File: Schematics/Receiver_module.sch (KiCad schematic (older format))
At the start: 17 parts, among them J1 I2C_ToTagger, T1 BC237, T2 BC237, T3 BC237

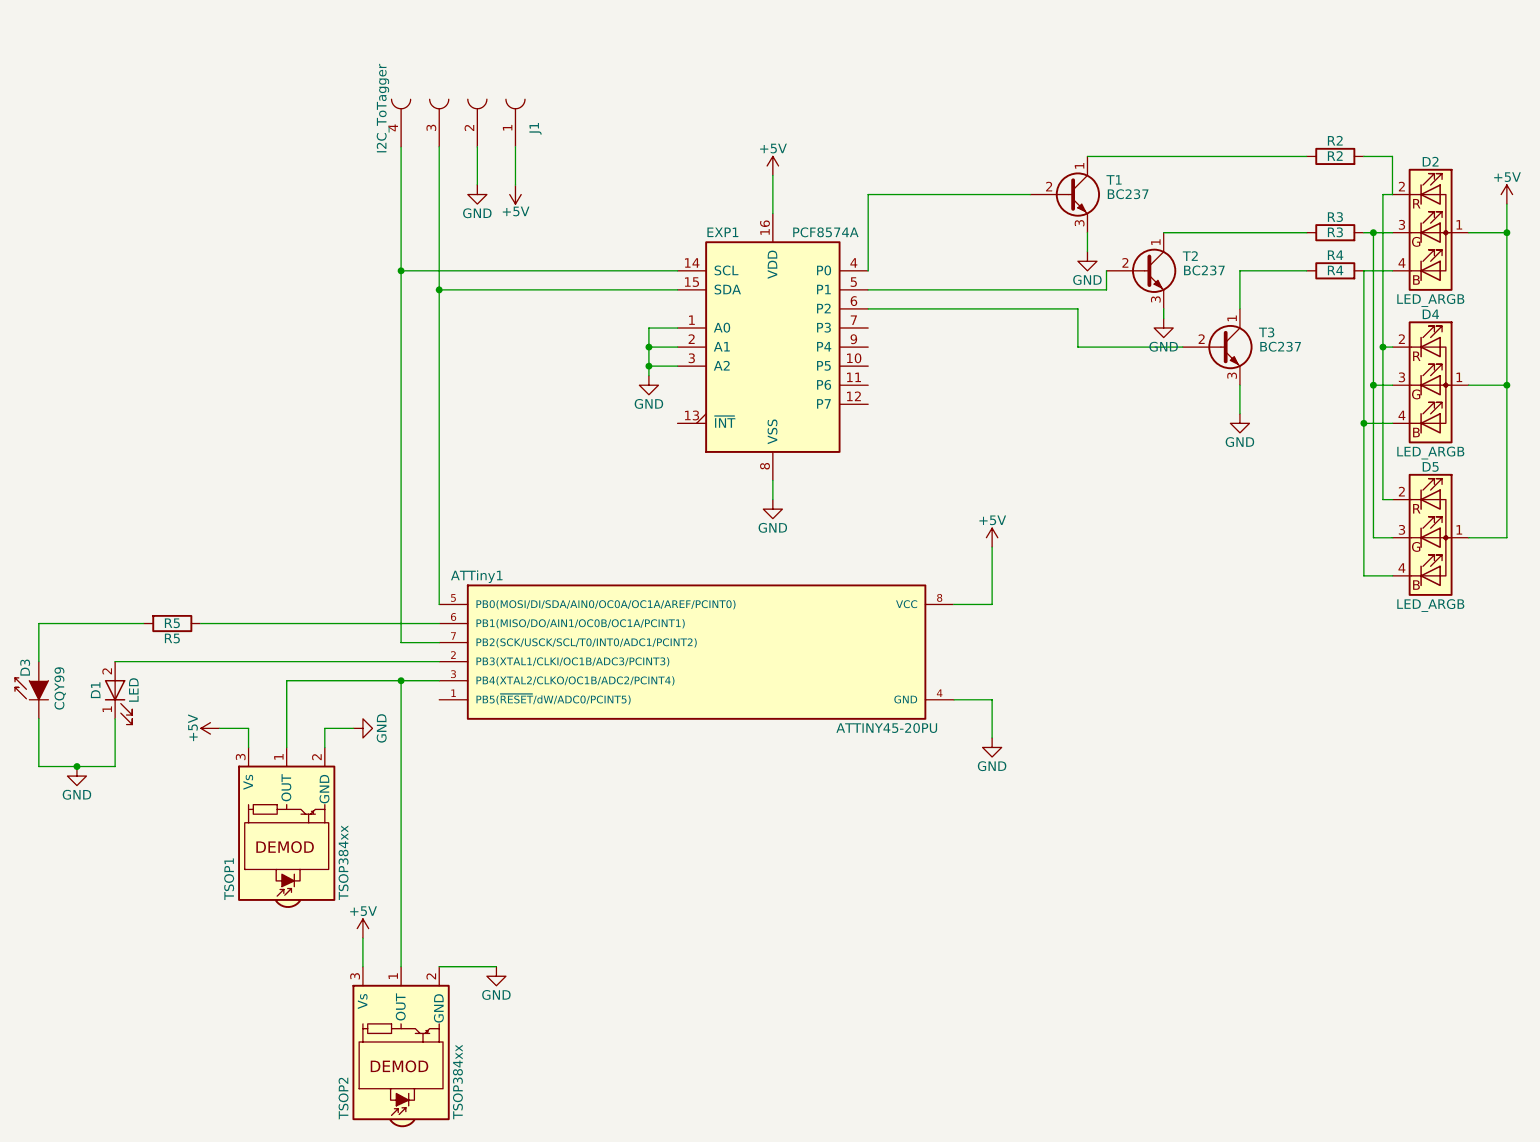
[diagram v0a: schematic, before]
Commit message: New Version of Tagger/Receiver Schematics and PCBs
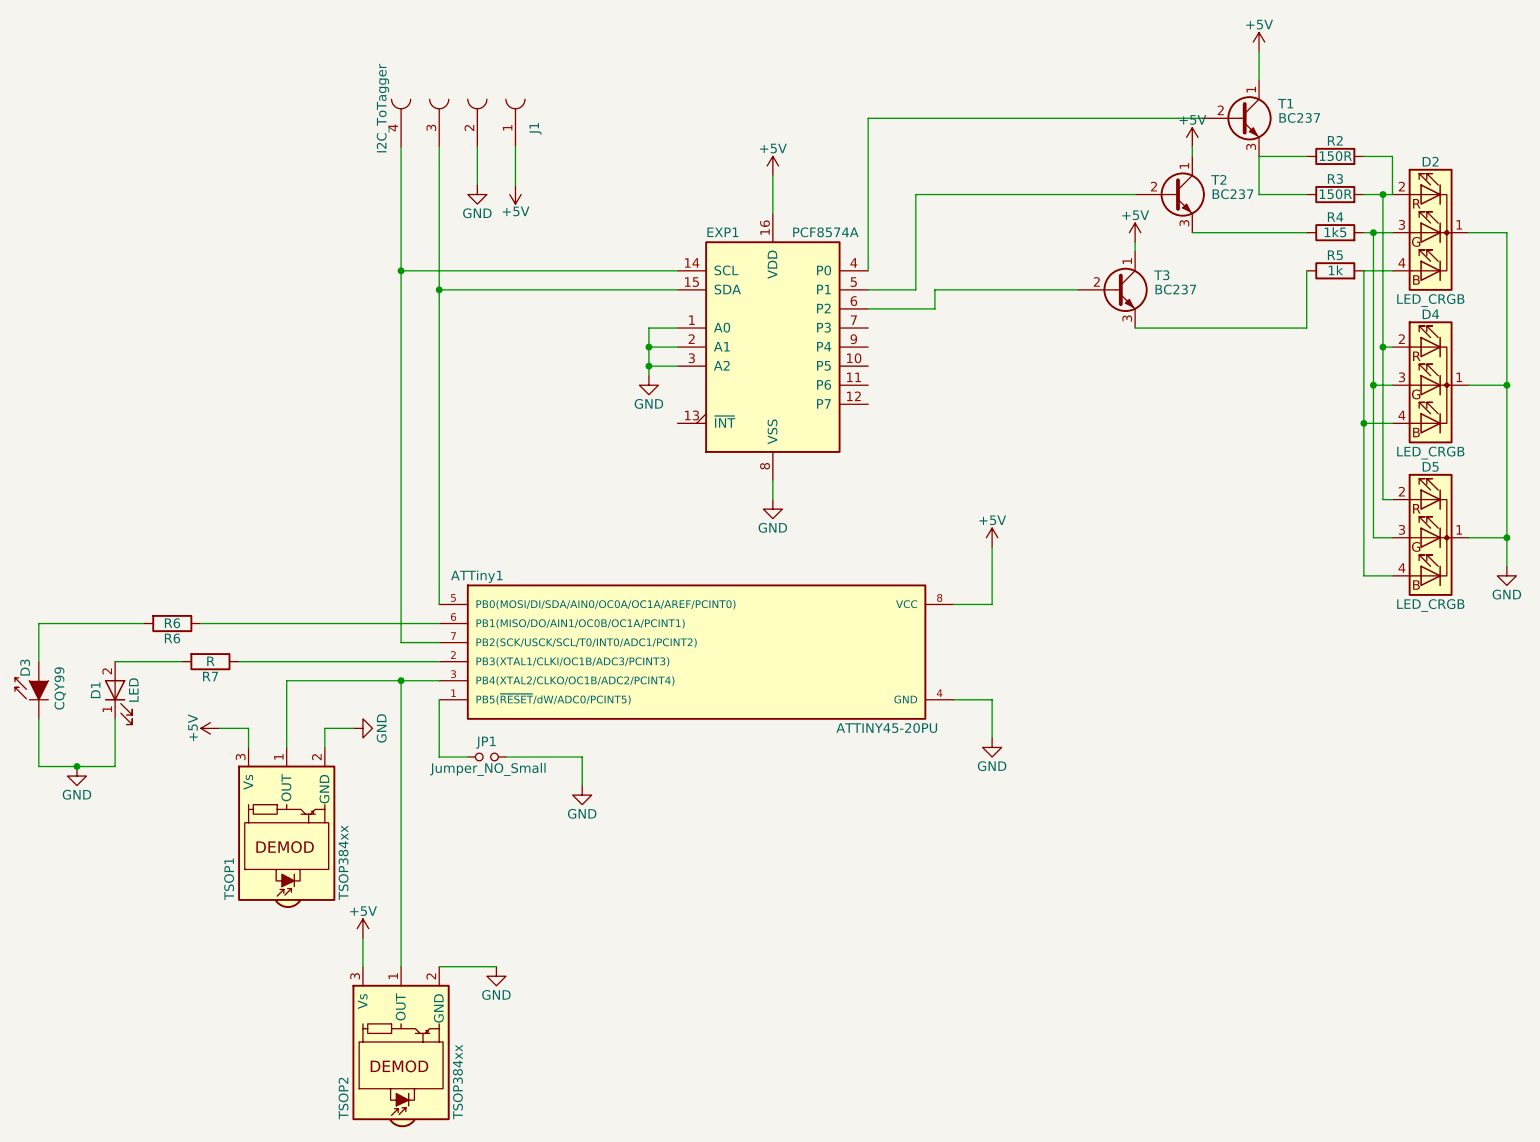
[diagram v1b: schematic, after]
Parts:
- removed D2, D4, D5: LED_ARGB, LEDs:LED_D5.0mm-4, symbol LED_ARGB
- added D2, D4, D5: LED_CRGB, RGB_LED_CC_5mm:LED_D5.0mm-4, symbol LED_CRGB
- added JP1: Jumper_NO_Small, Pin_Headers:Pin_Header_Straight_1x02_Pitch2.54mm, symbol Jumper_NO_Small
- added R3: 150R, Resistors_THT:R_Axial_DIN0204_L3.6mm_D1.6mm_P2.54mm_Vertical, symbol R
- added R7: R, Resistors_THT:R_Axial_DIN0204_L3.6mm_D1.6mm_P2.54mm_Vertical, symbol R
- R2: value R2 -> 150R
- R4: renamed from R3; value R3 -> 1k5
- R5: renamed from R4; value R4 -> 1k
- R6: renamed from R5; value R5 -> R6
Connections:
- net +5V: now also T1.1 (C), T2.1 (C), T3.1 (C)
- net GND: now also D2.1 (K), D4.1 (K), D5.1 (K), JP1.2; no longer T1.3 (E), T2.3 (E), T3.3 (E)
- net at ATTiny1.1 (PB5(~RESET~/dW/ADC0/PCINT5)): now also JP1.1
- net at ATTiny1.2 (PB3(XTAL1/CLKI/OC1B/ADC3/PCINT3)): now also R7.1; no longer D1.2 (A)
- net at R2.2: now also D2.2 (RA), D4.2 (RA), D5.2 (RA), R3.2
- net at R4.2: now also D2.3 (GA), D4.3 (GA), D5.3 (GA)
- net at R5.2: now also D2.4 (BA), D4.4 (BA), D5.4 (BA)
- net at R2.1: now also T1.3 (E), R3.1; no longer T1.1 (C)
- net at R4.1: now also T2.3 (E); no longer T2.1 (C)
- net at R5.1: now also T3.3 (E); no longer T3.1 (C)
- new net: D1.2 (A), R7.2
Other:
- moved on the sheet: T1, T2, T3
